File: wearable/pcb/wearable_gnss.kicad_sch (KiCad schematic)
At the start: 9 parts, among them IC1 TESEO-LIV3F, J3 Extension, J5 Conn_01x05_Pin

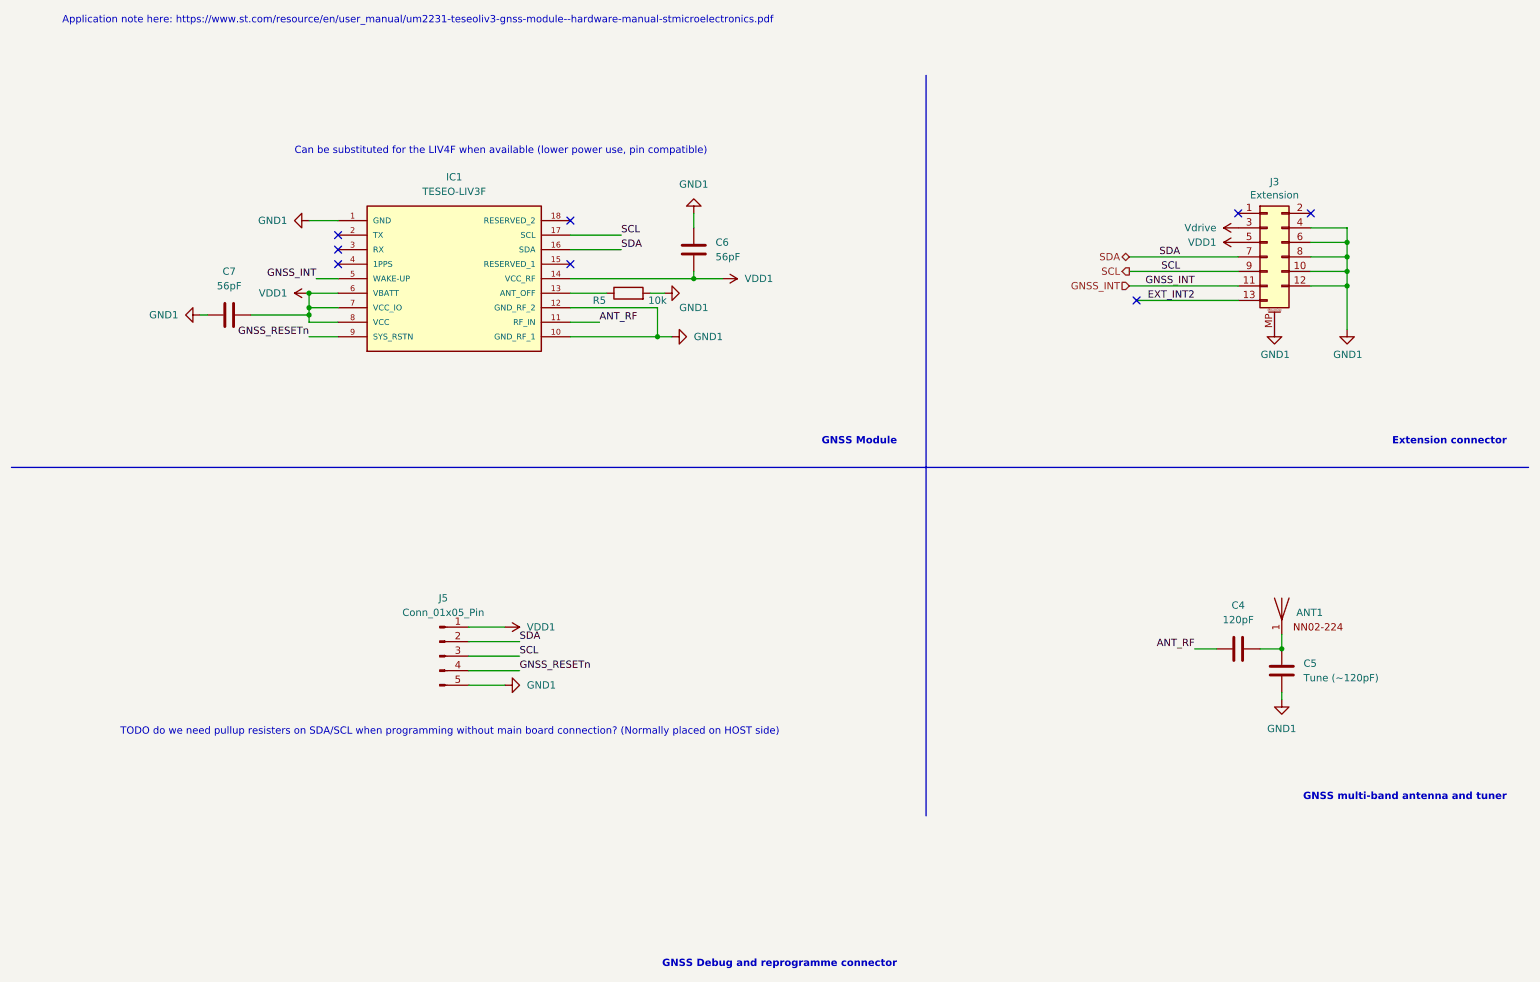
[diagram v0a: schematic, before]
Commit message: Part of #16. Added GNSS PCB layout
Also added custom footprint for NN02-224 chip antenna.
Signed-off-by: Adam Fowler <adam@adamfowler.org>
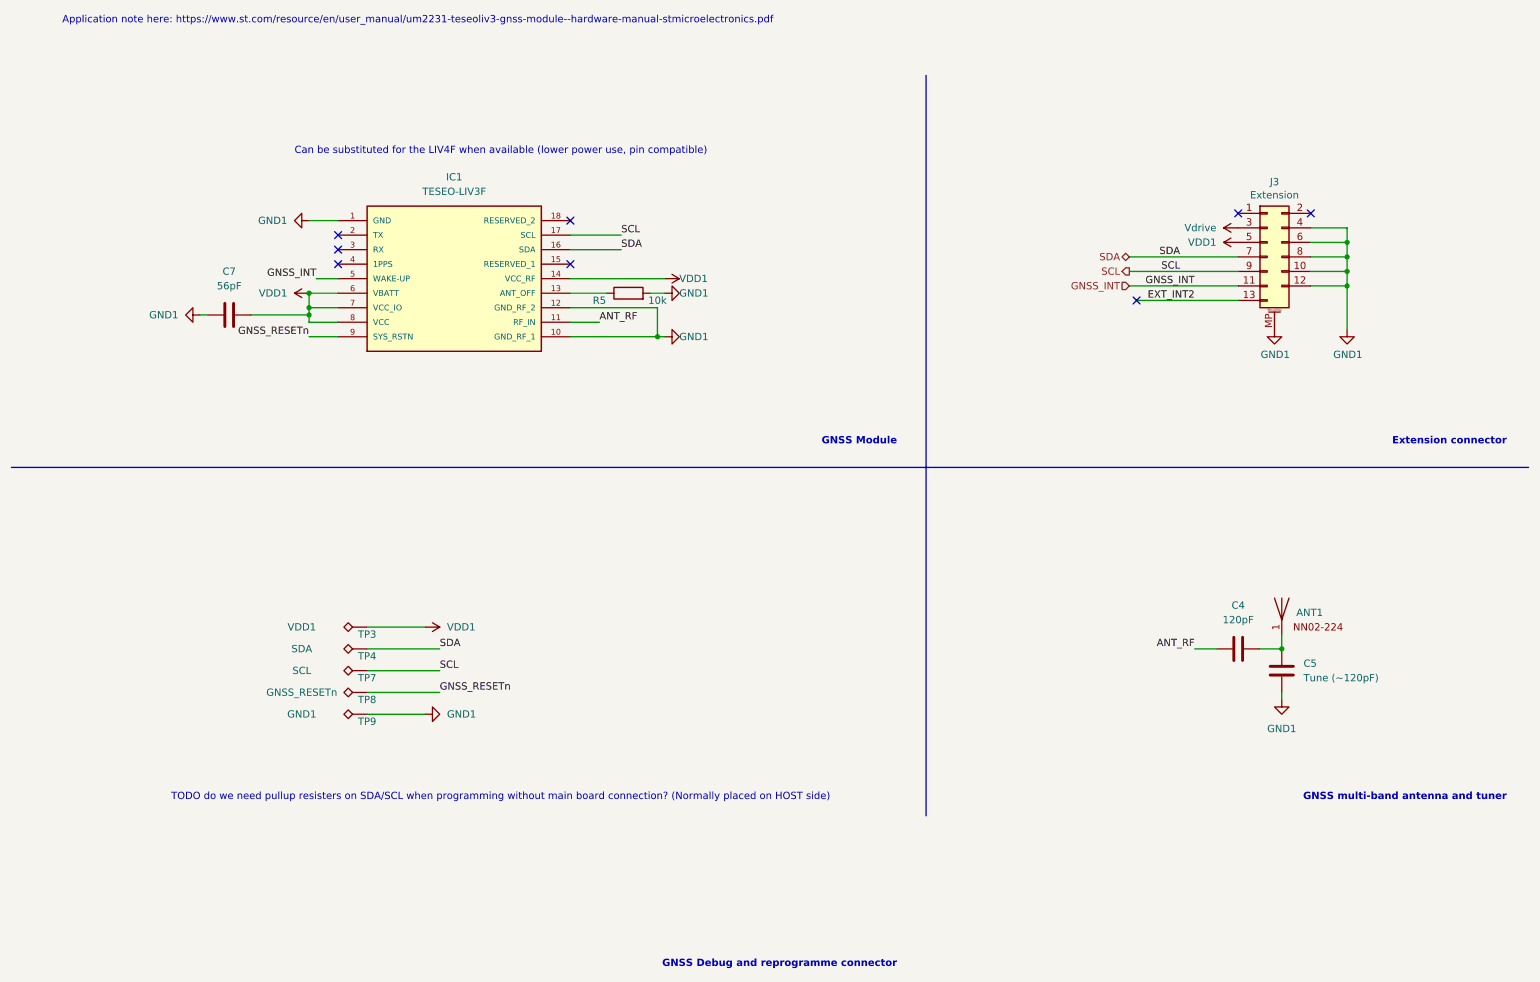
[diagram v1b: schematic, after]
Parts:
- removed C6: 56pF, symbol Device:C
- removed J5: Conn_01x05_Pin, symbol Connector:Conn_01x05_Pin
- added TP3: VDD1, TestPoint:TestPoint_Pad_D1.0mm, symbol Connector:TestPoint_Alt
- added TP4: SDA, TestPoint:TestPoint_Pad_D1.0mm, symbol Connector:TestPoint_Alt
- added TP7: SCL, TestPoint:TestPoint_Pad_D1.0mm, symbol Connector:TestPoint_Alt
- added TP8: GNSS_RESETn, TestPoint:TestPoint_Pad_D1.0mm, symbol Connector:TestPoint_Alt
- added TP9: GND1, TestPoint:TestPoint_Pad_D1.0mm, symbol Connector:TestPoint_Alt
- ANT1: footprint (none) -> Herald_Extras:NN02-224
- C4, C5, C7: footprint (none) -> Capacitor_SMD:C_0402_1005Metric
- IC1: footprint SON110P970X1010X230-18N -> Herald_Extras:SON110P970X1010X230-18N
- R5: footprint (none) -> Resistor_SMD:R_0402_1005Metric
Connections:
- net GND1: now also TP9.1
- net GNSS_RESETn: now also TP8.1
- net SCL: now also TP7.1
- net SDA: now also TP4.1
- net VDD1: now also TP3.1
